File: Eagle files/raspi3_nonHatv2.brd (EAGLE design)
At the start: 78.7 x 73.3 mm, 40 parts, among them IC5 PAM8403, K1 PIN20X2, X1 JST-XH-05-PIN-LONG-PAD, X2 JST-XH-02-PIN-LONG-PAD

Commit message: updated
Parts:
- removed J4: (no value), SparkFun-Connectors:MOLEX-1X4
- removed THERMISTOR1, THERMISTOR2, THERMISTOR3, THERMISTOR4: (no value), SparkFun-Connectors:MOLEX-1X2
- added X3, X4, X5: JST-XH-02-PIN-LONG-PAD, Rembrandt Electronics - JST XH Connectors v1-0:JST-XH-02-PACKAGE-LONG-PAD
- moved X1 88.3 mm to (5.71, 45.1), turned to 270 degrees
- moved X2 41.7 mm to (68.6, 19.7)
- moved C13 4.49 mm to (4.45, 10.8), turned to 270 degrees
- moved R8 2.54 mm to (15.2, 64.1)
- moved A1 2.54 mm to (3.81, 30.5)
- moved IC5 2.54 mm to (11.4, 15.2)
- moved C15 2.54 mm to (5.71, 16.5)
- moved C16 2.54 mm to (10.2, 21.6)
- moved C17 2.54 mm to (18.4, 16.5)
- moved C3 2.54 mm to (19.1, 57.8)
- moved C30 2.54 mm to (2.54, 17.8)
- moved C4 2.54 mm to (15.2, 58.4)
- moved R13 2.54 mm to (7.62, 62.2)
- moved R14 2.54 mm to (7.62, 64.8)
- moved R9 2.54 mm to (15.9, 61.6)
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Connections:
- net +3V3: now also X4.1; no longer THERMISTOR2.1
- net +5V: now also X5.1; no longer THERMISTOR3.1
- net AIN0: now also X1.4; no longer J4.1
- net AIN1: now also X1.3; no longer J4.2
- net AIN2: now also X1.2; no longer J4.3
- net AIN3: now also X1.1; no longer J4.4
- net GND: now also X1.5, X4.2, X5.2; no longer THERMISTOR2.2, THERMISTOR3.2
- net RX: now also X3.2; no longer THERMISTOR4.2
- net SCL: now also X2.1; no longer THERMISTOR1.1
- net SDA: now also X2.2; no longer THERMISTOR1.2
- net TX: now also X3.1; no longer THERMISTOR4.1
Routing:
- net GND: track 344.0 -> 358.0 mm
- net +5V: track 166.8 -> 163.1 mm
- net N$27: track 14.0 -> 11.1 mm
- net +3V3: track 219.3 -> 221.8 mm
- net N$4: track 9.14 -> 6.60 mm
- net TX: track 72.2 -> 69.9 mm
- net RX: track 77.4 -> 75.5 mm
- net AIN2: track 11.8 -> 13.6 mm
- net 1SCLK: track 50.8 -> 52.5 mm
- net AIN1: track 11.7 -> 13.2 mm
- net AIN3: track 11.8 -> 13.2 mm
- net AIN0: track 20.3 -> 20.8 mm
- net 1MOSI: track 67.0 -> 67.5 mm
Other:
- board text added: "GND"

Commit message: 8-eagle
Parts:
- removed J1, J2: (no value), SparkFun-Connectors:MOLEX-1X4
- added X6, X7: JST-XH-03-PIN-LONG-PAD, Rembrandt Electronics - JST XH Connectors v1-0:JST-XH-03-PACKAGE-LONG-PAD
- added X8, X9: JST-XH-05-PIN-LONG-PAD, Rembrandt Electronics - JST XH Connectors v1-0:JST-XH-05-PACKAGE-LONG-PAD
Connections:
- new net GND1: X8.5
- new net GND2: X9.5
- new net N$10: X6.3
- new net N$8: X6.1
- new net N$9: X6.2
- net 0CS0: now also X8.4; no longer J2.1
- net 0MISO: now also X8.1; no longer J2.4
- net 0MOSI: now also X8.2; no longer J2.3
- net 0SCLK: now also X8.3; no longer J2.2
- net 1CS0: now also X9.4; no longer J1.1
- net 1MISO: now also X9.1; no longer J1.4
- net 1MOSI: now also X9.2; no longer J1.3
- net 1SCLK: now also X9.3; no longer J1.2
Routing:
- net 1SCLK: track 52.5 -> 44.9 mm
- net 1MOSI: track 67.5 -> 61.8 mm
- net 1MISO: track 70.8 -> 67.0 mm
- net 0CS0: track 111.8 -> 108.0 mm
- net 1CS0: track 65.5 -> 63.0 mm
- net 0MISO: track 38.9 -> 37.1 mm
- net 0SCLK: track 41.1 -> 39.8 mm
- net 0MOSI: track 47.1 -> 45.8 mm
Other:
- board size 78.7 x 73.3 mm -> 78.7 x 77.1 mm

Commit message: raspi material added
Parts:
- removed POWER: (no value), SparkFun-Connectors:MOLEX-1X3
- removed X6: JST-XH-03-PIN-LONG-PAD, Rembrandt Electronics - JST XH Connectors v1-0:JST-XH-03-PACKAGE-LONG-PAD
- moved X7 76.8 mm to (68.6, 24.1), turned to 270 degrees
- moved X8 14.1 mm to (69.8, 38.7)
- moved X3 5.71 mm to (68.6, 5.71)
- moved X2 5.71 mm to (68.6, 14.0)
- moved X9 3.42 mm to (69.8, 71.8), turned to 90 degrees
- moved C3 3.18 mm to (19.1, 61.0)
- moved K1 3.18 mm to (29.2, 35.6)
- moved OLED_MODULE 3.18 mm to (52.1, 42.5)
- moved R13 3.18 mm to (7.62, 65.4)
- moved R2 3.18 mm to (53.3, 62.9)
- moved SL1 3.18 mm to (34.9, 47.0)
- moved U$3 3.18 mm to (8.89, 62.9)
- moved X4 3.18 mm to (68.6, 51.4)
- moved A1 3.18 mm to (3.81, 33.7)
- moved C13 3.18 mm to (4.45, 14.0)
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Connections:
- removed net GND1: X8.5
- removed net GND2: X9.5
- removed net N$10: X6.3
- removed net N$8: X6.1
- removed net N$9: X6.2
- net +3V3: now also X7.2; no longer POWER.2
- net +5V: now also X7.3; no longer POWER.3
- net GND: now also X7.1, X8.5, X9.5; no longer POWER.1
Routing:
- net GND: track 358.0 -> 445.2 mm
- net +5V: track 163.1 -> 187.2 mm
- net 1MOSI: track 61.8 -> 77.5 mm
- net 0CS0: track 108.0 -> 121.7 mm
- net 1SCLK: track 44.9 -> 54.4 mm
- net SCL: track 94.0 -> 103.2 mm
- net 1MISO: track 67.0 -> 76.2 mm
- net 0MOSI: track 45.8 -> 54.1 mm
- net TX: track 69.9 -> 61.7 mm
- net RX: track 75.5 -> 68.2 mm
- net 1CS0: track 63.0 -> 68.8 mm
- net +3V3: track 221.8 -> 226.2 mm
- net 0MISO: track 37.1 -> 41.2 mm
- net SDA: track 98.4 -> 98.9 mm
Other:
- board size 78.7 x 77.1 mm -> 78.7 x 80.3 mm

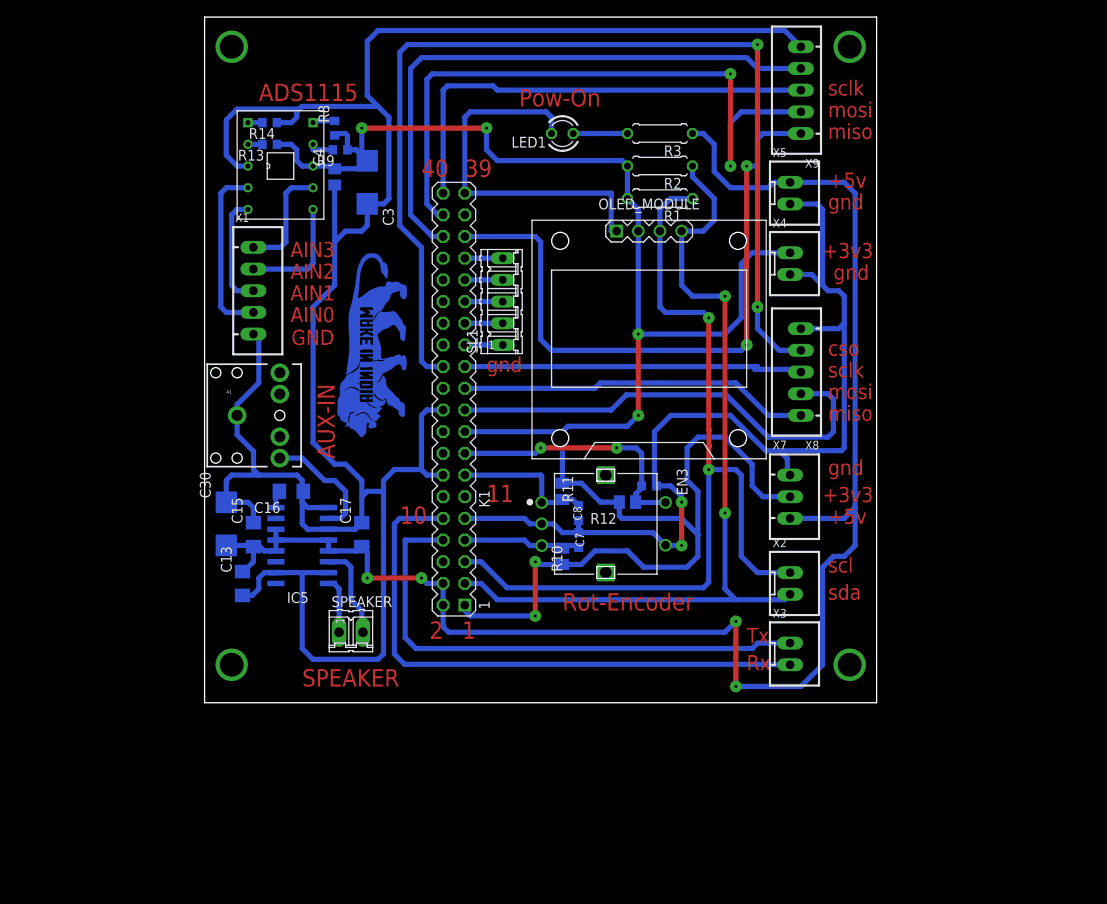
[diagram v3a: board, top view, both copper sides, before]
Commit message: color names updated
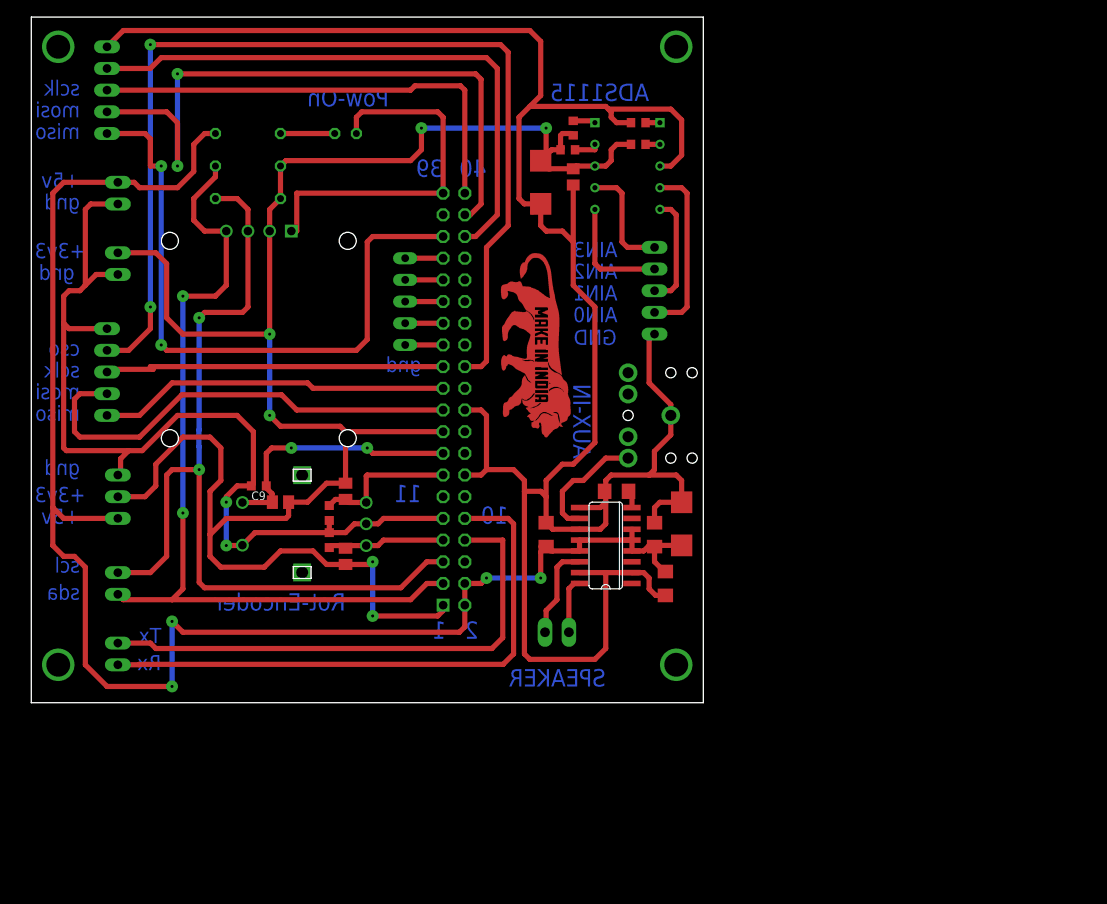
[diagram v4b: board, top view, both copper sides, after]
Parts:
- moved X8 81.3 mm to (-11.4, 38.7), flipped to the bottom
- moved X9 81.3 mm to (-11.4, 71.8), flipped to the bottom
- moved X2 78.7 mm to (-10.2, 14.0), flipped to the bottom
- moved X3 78.7 mm to (-10.2, 5.71), flipped to the bottom
- moved X4 78.7 mm to (-10.2, 51.4), flipped to the bottom
- moved X5 78.7 mm to (-10.2, 59.7), flipped to the bottom
- moved X7 78.7 mm to (-10.2, 24.1), flipped to the bottom
- moved C30 53.3 mm to (55.9, 21.0), flipped to the top
- moved A1 50.8 mm to (54.6, 33.7), flipped to the bottom
- moved C13 49.5 mm to (54.0, 14.0), flipped to the top
- moved R1 48.3 mm to (5.08, 59.1), flipped to the bottom
- moved R2 48.3 mm to (5.08, 62.9), flipped to the bottom
- moved R3 48.3 mm to (5.08, 66.7), flipped to the bottom
- moved C15 47.0 mm to (52.7, 19.7), flipped to the top
- moved X1 47.0 mm to (52.7, 48.3), flipped to the bottom
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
